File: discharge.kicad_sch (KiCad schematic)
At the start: 2 parts, among them K1 G5LE-1

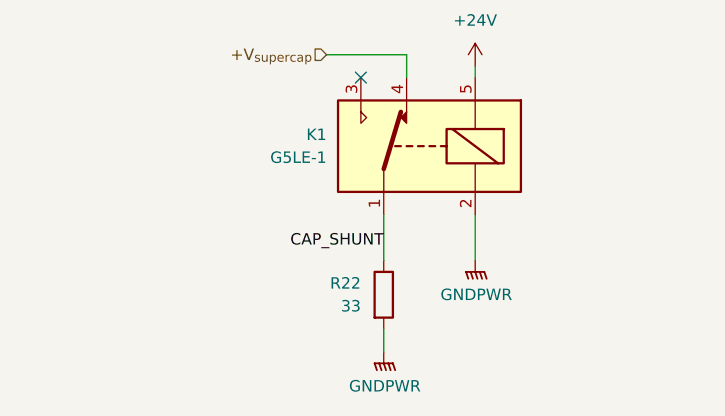
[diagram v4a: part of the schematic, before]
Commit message: Reannotate schematic
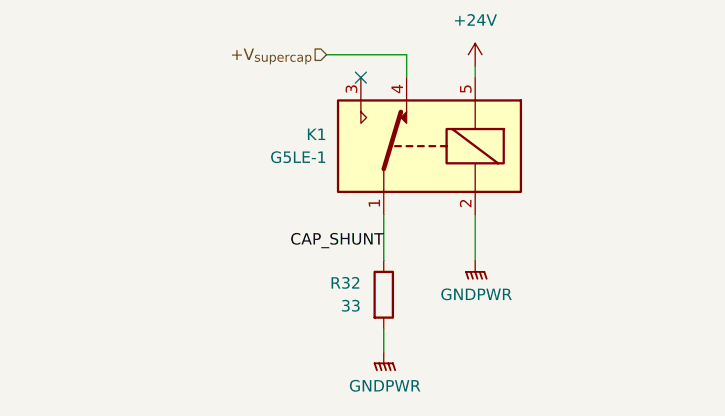
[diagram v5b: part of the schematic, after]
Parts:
- renumbered R22 to R32
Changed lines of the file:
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@@
 		(dnp no)
 		(fields_autoplaced yes)
-		(property "Reference" "#PWR042"
+		(property "Reference" "#PWR046"
 			(at 134.62 165.1 0)
 			(effects
@@
 			(project "SupercapManager"
 				(path "/6197145b-e7d4-44cc-9d90-537b6501bf60/ed9bb12b-3108-48de-97f5-99577caac45c"
-					(reference "#PWR042")
+					(reference "#PWR046")
 					(unit 1)
 				)
@@
 		(dnp no)
 		(fields_autoplaced yes)
-		(property "Reference" "#PWR040"
+		(property "Reference" "#PWR044"
 			(at 144.78 132.08 0)
 			(effects
@@
 			(project ""
 				(path "/6197145b-e7d4-44cc-9d90-537b6501bf60/ed9bb12b-3108-48de-97f5-99577caac45c"
-					(reference "#PWR040")
+					(reference "#PWR044")
 					(unit 1)
 				)
@@
 		(on_board yes)
 		(dnp no)
-		(property "Reference" "R22"
+		(property "Reference" "R32"
 			(at 132.08 152.3999 0)
 			(effects
@@
 			(project ""
 				(path "/6197145b-e7d4-44cc-9d90-537b6501bf60/ed9bb12b-3108-48de-97f5-99577caac45c"
-					(reference "R22")
+					(reference "R32")
 					(unit 1)
 				)
@@
 		(dnp no)
 		(fields_autoplaced yes)
-		(property "Reference" "#PWR041"
+		(property "Reference" "#PWR045"
 			(at 144.78 154.94 0)
 			(effects
@@
 			(project "SupercapManager"
 				(path "/6197145b-e7d4-44cc-9d90-537b6501bf60/ed9bb12b-3108-48de-97f5-99577caac45c"
-					(reference "#PWR041")
+					(reference "#PWR045")
 					(unit 1)
 				)

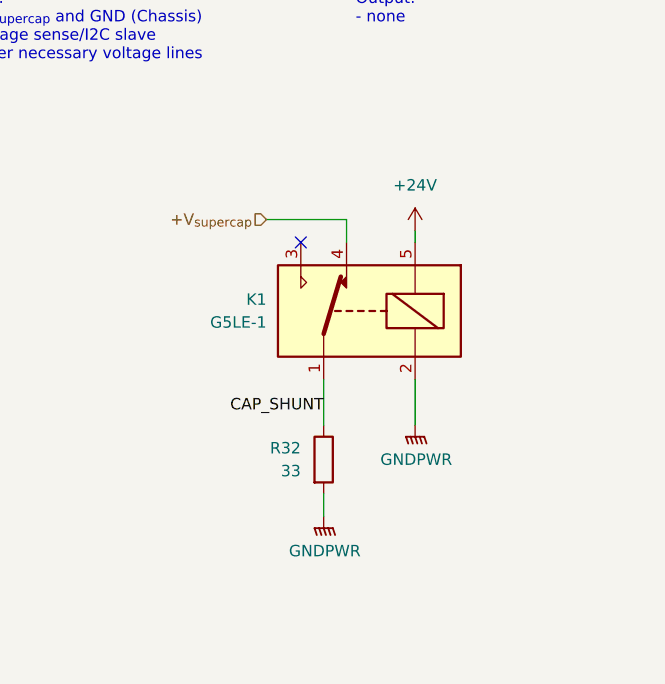
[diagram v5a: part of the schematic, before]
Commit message: Adjusted some things + changed discharge to have a smaller time constant
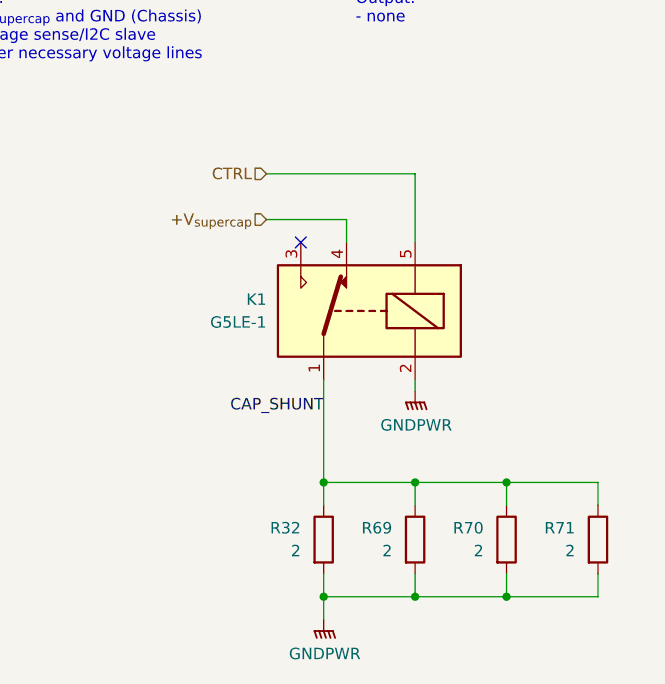
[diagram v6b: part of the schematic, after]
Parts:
- added R69, R70, R71: 2, symbol Device:R
- R32: value 33 -> 2; footprint Resistor_SMD:R_1210_3225Metric_Pad1.30x2.65mm_HandSolder -> (none); Mouser Part Number 603-AC1210JR-0733RL -> 708-KAL25FB2R00
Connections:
- net CAP_SHUNT: now also R69.1, R70.1, R71.1
- net GNDPWR: now also R69.2, R70.2, R71.2
- net +24V renamed CTRL
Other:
- moved on the sheet: R32

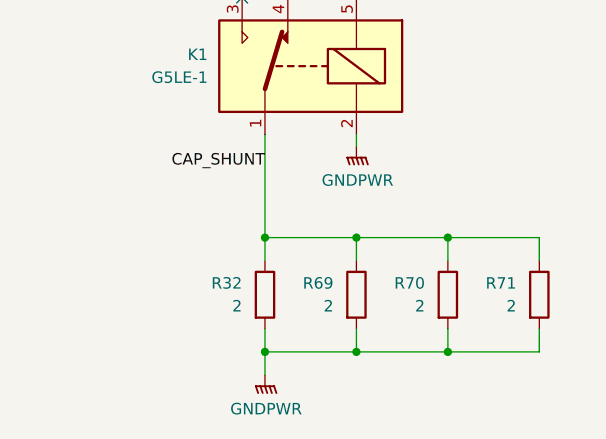
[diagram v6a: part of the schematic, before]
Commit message: Renumbering components
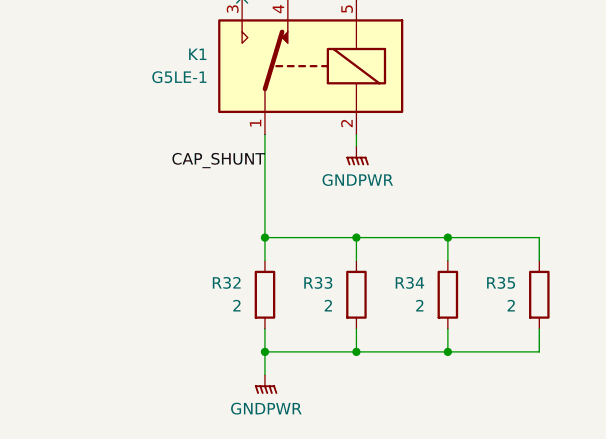
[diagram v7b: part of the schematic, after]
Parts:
- renumbered R69 to R33, R70 to R34, R71 to R35
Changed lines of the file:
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@@
 		(dnp no)
 		(fields_autoplaced yes)
-		(property "Reference" "#PWR046"
+		(property "Reference" "#PWR047"
 			(at 134.62 176.53 0)
 			(effects
@@
 			(project "SupercapManager"
 				(path "/6197145b-e7d4-44cc-9d90-537b6501bf60/ed9bb12b-3108-48de-97f5-99577caac45c"
-					(reference "#PWR046")
+					(reference "#PWR047")
 					(unit 1)
 				)
@@
 		(on_board yes)
 		(dnp no)
-		(property "Reference" "R71"
+		(property "Reference" "R35"
 			(at 162.56 161.2899 0)
 			(effects
@@
 			(project "SupercapManager"
 				(path "/6197145b-e7d4-44cc-9d90-537b6501bf60/ed9bb12b-3108-48de-97f5-99577caac45c"
-					(reference "R71")
+					(reference "R35")
 					(unit 1)
 				)
@@
 		(on_board yes)
 		(dnp no)
-		(property "Reference" "R70"
+		(property "Reference" "R34"
 			(at 152.4 161.2899 0)
 			(effects
@@
 			(project "SupercapManager"
 				(path "/6197145b-e7d4-44cc-9d90-537b6501bf60/ed9bb12b-3108-48de-97f5-99577caac45c"
-					(reference "R70")
+					(reference "R34")
 					(unit 1)
 				)
@@
 		(on_board yes)
 		(dnp no)
-		(property "Reference" "R69"
+		(property "Reference" "R33"
 			(at 142.24 161.2899 0)
 			(effects
@@
 			(project "SupercapManager"
 				(path "/6197145b-e7d4-44cc-9d90-537b6501bf60/ed9bb12b-3108-48de-97f5-99577caac45c"
-					(reference "R69")
+					(reference "R33")
 					(unit 1)
 				)
@@
 		(dnp no)
 		(fields_autoplaced yes)
-		(property "Reference" "#PWR045"
+		(property "Reference" "#PWR046"
 			(at 144.78 151.13 0)
 			(effects
@@
 			(project "SupercapManager"
 				(path "/6197145b-e7d4-44cc-9d90-537b6501bf60/ed9bb12b-3108-48de-97f5-99577caac45c"
-					(reference "#PWR045")
+					(reference "#PWR046")
 					(unit 1)
 				)

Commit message: Sourcing various parts
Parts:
- added J10: XT30_F, Connector_AMASS:AMASS_XT30U-F_1x02_P5.0mm_Vertical, symbol Connector:Conn_01x02_Pin
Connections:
- net CAP_SHUNT: now also J10.1 (Pin_1)
- net GNDPWR: now also J10.2 (Pin_2)
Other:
- note added: "Connector to power resistors"
- moved on the sheet: K1, R32, R33, R34, R35
